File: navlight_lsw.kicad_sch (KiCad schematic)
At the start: 7 parts, among them U16 TPS26400RHFR

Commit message: BOM in folder
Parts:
- C86: JLCPCB Status (none) -> JLC in-stock package match; Mfr P/N UMK107AB7105KA-T -> CL10A105KB8NNNC; Supplier_1 DigiKey -> LCSC; Supplier_1 P/N UMK107AB7105KA-T -> C15849; Supplier_1 Unit Price $0.08 -> (none)
- C87: Supplier_1 DigiKey -> LCSC; Supplier_1 P/N 1276-1000-2-ND -> C1591; Supplier_1 Unit Price $0.08 -> (none)
- R67: JLCPCB Status (none) -> Similar JLC in-stock package match; Mfr P/N RT0603BRE07402KL -> FRC0603F4023TS; Supplier_1 (none) -> LCSC; Supplier_1 P/N (none) -> C2960796
- R68: JLCPCB Status (none) -> JLC in-stock package match; Mfr P/N ERA-3AEB333V -> 0603WAF3302T5E; Supplier_1 Digikey -> LCSC; Supplier_1 P/N P33KDBTR-ND -> C4216; Supplier_1 Unit Price 0.10000 -> (none)
- R69, R70: JLCPCB Status (none) -> JLC in-stock package match; Mfr P/N RT0603BRD0712KL -> 0603WAF1202T5E; Supplier_1 Digikey -> LCSC; Supplier_1 P/N (none) -> C22790
- U16: JLCPCB Status (none) -> JLC in-stock package match; Mfr P/N (none) -> TPS26400RHFR; Supplier_1 (none) -> LCSC; Supplier_1 P/N (none) -> C2876715
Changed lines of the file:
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@@
 			)
 		)
-		(property "Mfr P/N" " RT0603BRD0712KL"
+		(property "Mfr P/N" "0603WAF1202T5E"
 			(at 181.61 113.03 0)
 			(effects
@@
 			)
 		)
-		(property "Supplier_1" "Digikey"
+		(property "Supplier_1" "LCSC"
 			(at 181.61 113.03 0)
 			(effects
@@
 			)
 		)
-		(property "Supplier_1 P/N" ""
+		(property "Supplier_1 P/N" "C22790"
 			(at 181.61 113.03 0)
 			(effects
@@
 		(property "Supplier_2 Price @ Qty" "1"
 			(at 181.61 113.03 0)
+			(effects
+				(font
+					(size 1.27 1.27)
+				)
+				(hide yes)
+			)
+		)
+		(property "JLCPCB Status" "JLC in-stock package match"
+			(at 181.61 113.03 270)
+			(effects
+				(font
+					(size 1.27 1.27)
+				)
+				(hide yes)
+			)
+		)
+		(property "SNAPEDA_PN" ""
+			(at 181.61 113.03 90)
 			(effects
 				(font
@@
 			)
 		)
-		(property "Mfr P/N" "RT0603BRE07402KL"
+		(property "Mfr P/N" "FRC0603F4023TS"
 			(at 119.38 107.95 0)
 			(effects
@@
 			)
 		)
-		(property "Supplier_1" ""
+		(property "Supplier_1" "LCSC"
 			(at 119.38 107.95 0)
 			(effects
@@
 			)
 		)
-		(property "Supplier_1 P/N" ""
+		(property "Supplier_1 P/N" "C2960796"
 			(at 119.38 107.95 0)
 			(effects
@@
 		(property "Supplier_2 Price @ Qty" "1"
 			(at 119.38 107.95 0)
+			(effects
+				(font
+					(size 1.27 1.27)
+				)
+				(hide yes)
+			)
+		)
+		(property "JLCPCB Status" "Similar JLC in-stock package match"
+			(at 119.38 107.95 90)
+			(effects
+				(font
+					(size 1.27 1.27)
+				)
+				(hide yes)
+			)
+		)
+		(property "SNAPEDA_PN" ""
+			(at 119.38 107.95 90)
 			(effects
 				(font
@@
 			)
 		)
-		(property "Mfr P/N" "ERA-3AEB333V"
+		(property "Mfr P/N" "0603WAF3302T5E"
 			(at 181.61 97.79 0)
 			(effects
@@
 			)
 		)
-		(property "Supplier_1" "Digikey"
+		(property "Supplier_1" "LCSC"
 			(at 181.61 97.79 0)
 			(effects
@@
 			)
 		)
-		(property "Supplier_1 P/N" "P33KDBTR-ND"
+		(property "Supplier_1 P/N" "C4216"
 			(at 181.61 97.79 0)
 			(effects
@@
 			)
 		)
-		(property "Supplier_1 Unit Price" "0.10000"
+		(property "Supplier_1 Unit Price" ""
 			(at 181.61 97.79 0)
 			(effects
@@
 		(property "Supplier_2 Price @ Qty" "1"
 			(at 181.61 97.79 0)
+			(effects
+				(font
+					(size 1.27 1.27)
+				)
+				(hide yes)
+			)
+		)
+		(property "JLCPCB Status" "JLC in-stock package match"
+			(at 181.61 97.79 270)
+			(effects
+				(font
+					(size 1.27 1.27)
+				)
+				(hide yes)
+			)
+		)
+		(property "SNAPEDA_PN" ""
+			(at 181.61 97.79 90)
 			(effects
 				(font
@@
 			)
 		)
-		(property "Supplier_1" "DigiKey"
+		(property "Supplier_1" "LCSC"
 			(at 119.38 113.03 0)
 			(effects
@@
 			)
 		)
-		(property "Supplier_1 P/N" "1276-1000-2-ND"
+		(property "Supplier_1 P/N" "C1591"
 			(at 119.38 113.03 0)
 			(effects
@@
 			)
 		)
-		(property "Supplier_1 Unit Price" "$0.08"
+		(property "Supplier_1 Unit Price" ""
 			(at 119.38 113.03 0)
 			(effects
@@
 		(property "Supplier_2_Price @ QTY" "1"
 			(at 119.38 113.03 0)
+			(effects
+				(font
+					(size 1.27 1.27)
+				)
+				(hide yes)
+			)
+		)
+		(property "SNAPEDA_PN" ""
+			(at 119.38 113.03 90)
 			(effects
 				(font
@@
 			)
 		)
-		(property "Mfr P/N" "UMK107AB7105KA-T"
+		(property "Mfr P/N" "CL10A105KB8NNNC"
 			(at 82.55 91.44 0)
 			(effects
@@
 			)
 		)
-		(property "Supplier_1" "DigiKey"
+		(property "Supplier_1" "LCSC"
 			(at 82.55 91.44 0)
 			(effects
@@
 			)
 		)
-		(property "Supplier_1 P/N" "UMK107AB7105KA-T"
+		(property "Supplier_1 P/N" "C15849"
 			(at 82.55 91.44 0)
 			(effects
@@
 			)
 		)
-		(property "Supplier_1 Unit Price" "$0.08"
+		(property "Supplier_1 Unit Price" ""
 			(at 82.55 91.44 0)
 			(effects
@@
 		)
 		(property "Supplier_2_Price @ QTY" "1"
+			(at 82.55 91.44 0)
+			(effects
+				(font
+					(size 1.27 1.27)
+				)
+				(hide yes)
+			)
+		)
+		(property "JLCPCB Status" "JLC in-stock package match"
+			(at 82.55 91.44 0)
+			(effects
+				(font
+					(size 1.27 1.27)
+				)
+				(hide yes)
+			)
+		)
+		(property "SNAPEDA_PN" ""
 			(at 82.55 91.44 0)
 			(effects
@@
 			)
 		)
-		(property "Mfr P/N" ""
-			(at 130.81 87.63 0)
-			(effects
-				(font
-					(size 1.27 1.27)
-				)
-				(hide yes)
-			)
-		)
-		(property "Supplier_1" ""
-			(at 130.81 87.63 0)
-			(effects
-				(font
-					(size 1.27 1.27)
-				)
-				(hide yes)
-			)
-		)
-		(property "Supplier_1 P/N" ""
+		(property "Mfr P/N" "TPS26400RHFR"
+			(at 130.81 87.63 0)
+			(effects
+				(font
+					(size 1.27 1.27)
+				)
+				(hide yes)
+			)
+		)
+		(property "Supplier_1" "LCSC"
+			(at 130.81 87.63 0)
+			(effects
+				(font
+					(size 1.27 1.27)
+				)
+				(hide yes)
+			)
+		)
+		(property "Supplier_1 P/N" "C2876715"
 			(at 130.81 87.63 0)
 			(effects
@@
 		)
 		(property "Supplier_2 Price @ Qty" ""
+			(at 130.81 87.63 0)
+			(effects
+				(font
+					(size 1.27 1.27)
+				)
+				(hide yes)
+			)
+		)
+		(property "JLCPCB Status" "JLC in-stock package match"
+			(at 130.81 87.63 0)
+			(effects
+				(font
+					(size 1.27 1.27)
+				)
+				(hide yes)
+			)
+		)
+		(property "SNAPEDA_PN" ""
 			(at 130.81 87.63 0)
 			(effects
@@
 			)
 		)
-		(property "Mfr P/N" " RT0603BRD0712KL"
+		(property "Mfr P/N" "0603WAF1202T5E"
 			(at 181.61 107.95 0)
 			(effects
@@
 			)
 		)
-		(property "Supplier_1" "Digikey"
+		(property "Supplier_1" "LCSC"
 			(at 181.61 107.95 0)
 			(effects
@@
 			)
 		)
-		(property "Supplier_1 P/N" ""
+		(property "Supplier_1 P/N" "C22790"
 			(at 181.61 107.95 0)
 			(effects
@@
 			(effects
 				(font
+					(size 1.27 1.27)
+				)
+				(hide yes)
+			)
+		)
+		(property "JLCPCB Status" "JLC in-stock package match"
+			(at 181.61 107.95 270)
+			(effects
+				(font
+					(size 1.27 1.27)
+				)
+				(hide yes)
+			)
+		)
+		(property "SNAPEDA_PN" ""
+			(at 181.61 107.95 90)
+			(effects
+				(font

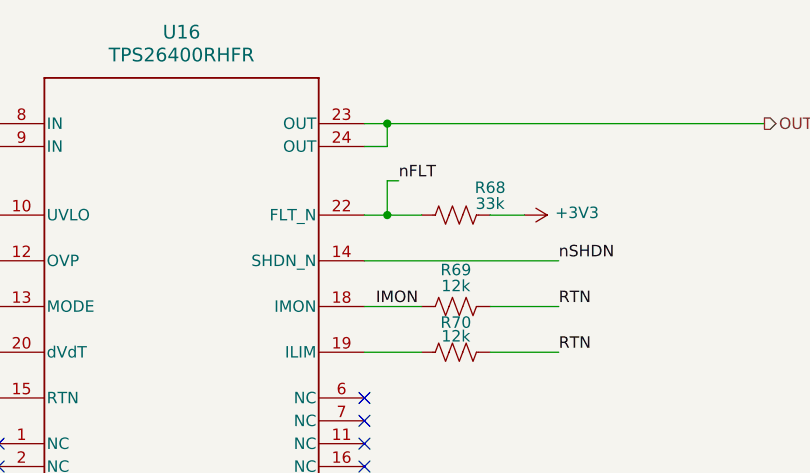
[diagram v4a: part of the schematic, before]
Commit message: Schematic updates
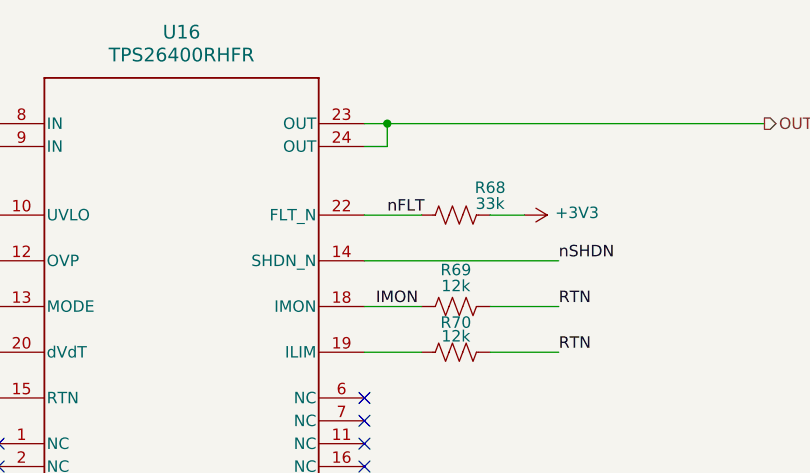
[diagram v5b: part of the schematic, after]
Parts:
- R69, R70: Mfr YAGEO -> UNI-ROYAL(Uniroyal Elec)
- U16: footprint _PowerBoard:RHF0024A-MFG -> RHF0024A-IPC_A
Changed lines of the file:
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@@
-		(color 0 0 0 0)
-	)
-	(junction
-		(at 173.99 97.79)
-		(diameter 0)
 		(color 0 0 0 0)
 	)
@@
 	(wire
 		(pts
-			(xy 171.45 97.79) (xy 173.99 97.79)
-		)
-		(stroke
-			(width 0)
-			(type default)
-		)
-	)
-	(wire
-		(pts
-			(xy 173.99 93.98) (xy 173.99 97.79)
+			(xy 171.45 97.79) (xy 177.8 97.79)
 		)
 		(stroke
@@
 	(wire
 		(pts
-			(xy 177.8 97.79) (xy 173.99 97.79)
-		)
-		(stroke
-			(width 0)
-			(type default)
-		)
-	)
-	(wire
-		(pts
 			(xy 109.22 97.79) (xy 127 97.79)
 		)
@@
 		(pts
 			(xy 127 102.87) (xy 130.81 102.87)
-		)
-		(stroke
-			(width 0)
-			(type default)
-		)
-	)
-	(wire
-		(pts
-			(xy 173.99 93.98) (xy 175.26 93.98)
 		)
 		(stroke
@@
 	)
 	(label "nFLT"
-		(at 175.26 93.98 0)
+		(at 173.99 97.79 0)
 		(effects
 			(font
@@
 			)
 		)
-		(property "Mfr" "YAGEO"
+		(property "Mfr" "UNI-ROYAL(Uniroyal Elec)"
 			(at 181.61 113.03 0)
 			(effects
@@
 			)
 		)
+		(property "Supplier_1 Price @ Qty" ""
+			(at 82.55 91.44 0)
+			(effects
+				(font
+					(size 1.27 1.27)
+				)
+				(hide yes)
+			)
+		)
+		(property "Supplier_2 Price @ Qty" ""
+			(at 82.55 91.44 0)
+			(effects
+				(font
+					(size 1.27 1.27)
+				)
+				(hide yes)
+			)
+		)
 		(pin "1"
 		)
@@
 			)
 		)
-		(property "Footprint" "_PowerBoard:RHF0024A-MFG"
+		(property "Footprint" "RHF0024A-IPC_A"
 			(at 130.81 87.63 0)
 			(effects
@@
 			)
 		)
-		(property "Mfr" "YAGEO"
+		(property "Mfr" "UNI-ROYAL(Uniroyal Elec)"
 			(at 181.61 107.95 0)
 			(effects
